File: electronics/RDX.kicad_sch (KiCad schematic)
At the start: 47 parts

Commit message: updating electronics to fit new outline
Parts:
- removed OUT.POW: Conn_01x06, symbol Connector_Generic:Conn_01x06
- added A7.J1_1, A7.J1_2, A7.J1_3: Anderson SB50, symbol Connector_Generic:Conn_01x02
- A6.J1_1: renamed from OUT.SV1; value Conn_01x03 -> GX12-3
- A6.J1_2: renamed from OUT.SV2; value Conn_01x03 -> GX12-3
- A6.J1_3: renamed from OUT.SV3; value Conn_01x03 -> GX12-3
- A6.J1_4: renamed from OUT.SV4; value Conn_01x03 -> GX12-3
- A6.J1_5: renamed from OUT.SV5; value Conn_01x03 -> GX12-3
- A6.J1_6: renamed from OUT.SV6; value Conn_01x03 -> GX12-3
- A9.J1_1: renamed from OUT.STEP1; value Conn_01x04 -> GX16-4
- renumbered A4.J1_21 to A4.J1_3, A4.J1_21 to A4.J1_4, PSU.J31 to A4.J1_5, PSU.J32 to A4.J1_6, PSU.J41 to A4.J2_1, A4.J12 to A4.J3_2, A4.PS11 to A4.PS1, A4.PS12 to A4.PS2, A4.PS13 to A4.PS3, OUT.IO1 to A5.J1_1, OUT.IO2 to A5.J1_2, OUT.MISC to A5.J1_3, OUT.SW2 to A8.SW1, OUT.SW1 to A8.SW2, OUT.U1 to A8.U1, OUT.STEP2 to A9.J1_2, OUT.STEP3 to A9.J1_3, OUT.STEP4 to A9.J1_4, PSU.J1 to J1, OUT.M1 to M1, A4.PS1 to PS1, PSU.SW1 to SW1
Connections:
- net +12V: now also A7.J1_2.1 (Pin_1)
- net +36V: now also A7.J1_1.1 (Pin_1)
- net 5V_PWR: now also A7.J1_3.1 (Pin_1)
- net GND: now also A7.J1_1.2 (Pin_2), A7.J1_2.2 (Pin_2), A7.J1_3.2 (Pin_2)
- new net: A2.J1_2., A2.U1_2. (B2) (x3)
- new net: A2.J1_4., A2.U1_4. (B2) (x3)
- new net: A2.J1_1., A2.U1_1. (B2) (x3)
- new net: A2.J1_3., A2.U1_3. (B2) (x3)
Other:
- note added: "A4.J1_3 (12V)"
- note added: "A4.J2_1 (5V)"
- note added: "A4.J3_1 (36V)"
- note added: "A5 - GPIO Connectors"
- note added: "A5.J1_2 - Special functions"
- note added: "A5.J1_3 - Special functions"
- note added: "A7 - Power connector"
- note added: "A8 - Input panel"
- note added: "Main PSU (A4.PS1) supports up to 3 connections"
- note removed: "IO2 - Special functions"
- note removed: "MISC - Special functions"
- note removed: "Main PSU (PSU.PS1) supports up to 3 connections"
- note removed: "PSU.J12 (36V)"
- note removed: "PSU.J22 (12V)"
- note removed: "PSU.J32 (5V)"
- moved on the sheet: A5.J1_1, A5.J1_2, A5.J1_3, A6.J1_1, A6.J1_2, A6.J1_3, A6.J1_4, A6.J1_5, A6.J1_6, A8.U1, M1

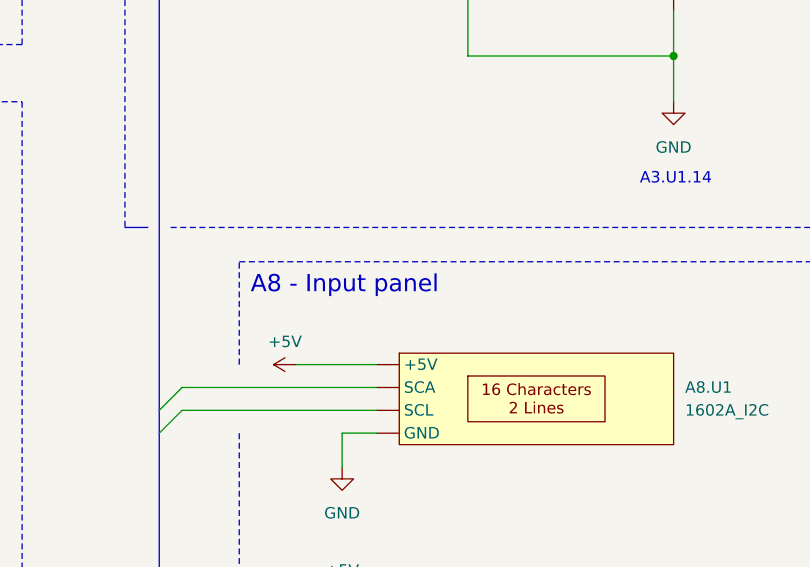
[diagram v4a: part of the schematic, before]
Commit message: first addition of screws
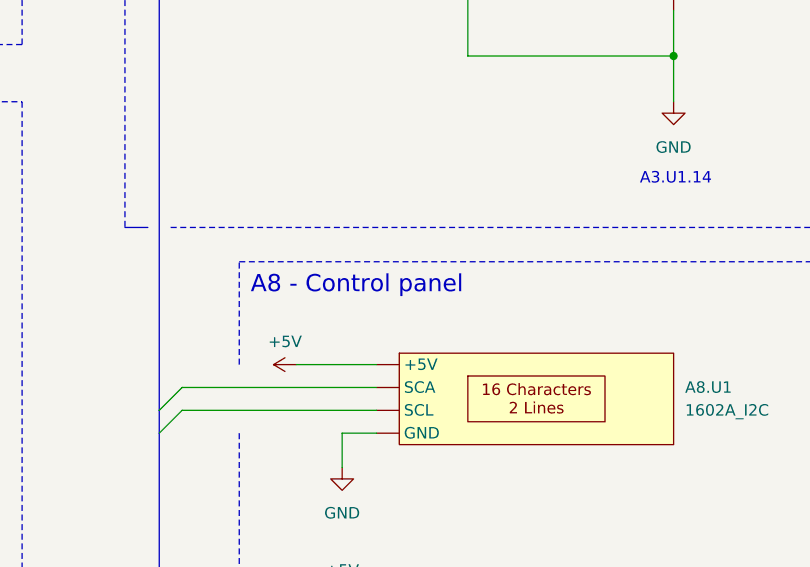
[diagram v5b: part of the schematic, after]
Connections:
- new net: A2.J1_2., A2.U1_2. (B2) (x3)
- new net: A2.J1_4., A2.U1_4. (B2) (x3)
- new net: A2.J1_1., A2.U1_1. (B2) (x3)
- new net: A2.J1_3., A2.U1_3. (B2) (x3)
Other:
- note added: "A8 - Control panel"
- note removed: "A8 - Input panel"
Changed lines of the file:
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@@
 		(title "RDX - Robot Driver Mk.X")
 		(date "2026-04-01")
-		(rev "1.2.0")
+		(rev "1.2.1")
 		(company "CornerLab")
 		(comment 1 "Universal Robot Driver")
@@
 		)
 	)
-	(text "A8 - Input panel"
+	(text "A8 - Control panel"
 		(exclude_from_sim no)
 		(at 191.77 203.454 0)

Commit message: schematics and electronics cleanup
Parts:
- removed A6.J1_1, A6.J1_2, A6.J1_3, A6.J1_4, A6.J1_5, A6.J1_6: GX12-3, symbol Connector_Generic:Conn_01x03
- removed A8.SW1: SW_SPST, symbol Switch:SW_SPST
- removed A9.J1_1: GX16-4, symbol Connector_Generic:Conn_01x04
- removed A9.J1_2, A9.J1_3, A9.J1_4: Conn_01x04, symbol Connector_Generic:Conn_01x04
- removed M1: Fan_4pin, symbol Motor:Fan_4pin
- added A10.J1_1, A10.J1_2, A10.J1_3: GX16-2, symbol Connector:Conn_01x02_Pin
- added A11.J1_1, A11.J1_2, A11.J1_3, A11.J1_4: GX16-4, symbol Connector:Conn_01x04_Pin
- added A3.J2, A3.J3: ~, symbol RDX_Comp:Conn_01-02
- added A3.J3_1: ~, symbol RDX_Comp:Conn_01-04
- added A5.U1_1, A5.U1_2: JoyIt-MotorDriver2, symbol RDX_Comp:JoyIt-MotorDriver2
- added A6.J1_1, A6.J1_2, A6.J1_3, A6.J1_4, A6.J1_5, A6.J1_6, A6.J1_7, A6.J1_8: GX12-3, symbol Connector:Conn_01x03_Pin
- added M1: Fan_3pin, symbol Motor:Fan_3pin
- renumbered A3.J3 to A3.J3_2, A4.PS1 to A4.PS1_1, A4.PS2 to A4.PS1_2, A4.PS3 to A4.PS2, A5.J1_1 to A6.J1_1, A5.J1_2 to A6.J1_2, A5.J1_3 to A6.J1_3
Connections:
- net MISC_5V is gone; now on net +5V: A3.U1.4 (+5V), A6.J1_3.1
- net +12V: now also A5.U1_2. (B2)
- net +36V: now also A3.J2.
- net 5V_PWR: now also A6.J1_1.2 (Pin_2), A6.J1_2.2 (Pin_2), A6.J1_3.2 (Pin_2), A6.J1_4.2 (Pin_2), A6.J1_5.2 (Pin_2), A6.J1_6.2 (Pin_2), A6.J1_7.2 (Pin_2), A6.J1_8.2 (Pin_2)
- net GND: now also A3.J3., A5.U1_2. (B2), A6.J1_1.3 (Pin_3), A6.J1_2.3 (Pin_3), A6.J1_3.3 (Pin_3), A6.J1_4.3 (Pin_3), A6.J1_5.3 (Pin_3), A6.J1_6.3 (Pin_3), A6.J1_7.3 (Pin_3), A6.J1_8.3 (Pin_3)
- net SC_EN: now also A3.J3_1.; no longer A3.U1.29 (IO5)
- net at A3.U2.9 (LED3): now also A6.J1_4.1 (Pin_1)
- net at A4.J1_1., A4.PS1_1.3 (+VIN), PS1.3 (DC+): now also A4.J3_1.
- net at A3.U2.10 (LED4): now also A6.J1_5.1 (Pin_1)
- net at A3.U2.11 (LED5): now also A6.J1_6.1 (Pin_1)
- net at A3.U2.12 (LED6): now also A6.J1_7.1 (Pin_1)
- net at A3.U2.13 (LED7): now also A6.J1_8.1 (Pin_1)
- net DC1_FW: now reaches A3.U2.15 (LED8)
- net DC1_FW: now also A5.U1_1. (B2)
- net DC1_BW: now reaches A3.U2.16 (LED9)
- net DC1_BW: now also A5.U1_1. (B2)
- net DC2_FW: now reaches A3.U2.17 (LED10)
- net DC2_FW: now also A5.U1_1. (B2)
- net DC2_BW: now reaches A3.U2.18 (LED11)
- net DC2_BW: now also A5.U1_1. (B2)
- net DC3_FW: now reaches A3.U2.19 (LED12)
- net DC3_FW: now also A5.U1_2. (B2)
- net DC3_BW: now reaches A3.U2.20 (LED13)
- net DC3_BW: now also A5.U1_2. (B2)
- net FAN_FW: now reaches A3.U2.21 (LED14)
- net FAN_FW: now also A5.U1_2. (B2)
- net FAN_BW: now reaches A3.U2.22 (LED15)
- net FAN_BW: now also A5.U1_2. (B2)
- net at A3.U2.6 (LED0): now also A6.J1_1.1 (Pin_1)
- net at A3.U2.7 (LED1): now also A6.J1_2.1 (Pin_1)
- net at A3.U2.8 (LED2): now also A6.J1_3.1 (Pin_1)
- new net: A11.J1_4.1 (Pin_1), A2.U1_4. (B2)
- new net: A11.J1_4.2 (Pin_2), A2.U1_4. (B2)
- new net: A11.J1_4.3 (Pin_3), A2.U1_4. (B2)
- new net: A11.J1_4.4 (Pin_4), A2.U1_4. (B2)
- new net: A11.J1_3.1 (Pin_1), A2.U1_3. (B2)
- new net: A11.J1_3.2 (Pin_2), A2.U1_3. (B2)
- new net: A11.J1_3.3 (Pin_3), A2.U1_3. (B2)
- new net: A11.J1_3.4 (Pin_4), A2.U1_3. (B2)
- new net: A2.J1_2., A2.U1_2. (B2) (x3)
- new net: A2.J1_4., A2.U1_4. (B2) (x3)
- new net: A10.J1_1.1 (Pin_1), A5.U1_1. (B2)
- new net: A10.J1_1.2 (Pin_2), A5.U1_1. (B2)
- new net: A10.J1_2.1 (Pin_1), A5.U1_1. (B2)
- new net: A10.J1_2.2 (Pin_2), A5.U1_1. (B2)
- new net: A3.J3., A5.U1_1. (B2)
- new net: A3.J2., A5.U1_1. (B2)
- new net: A2.J1_1., A2.U1_1. (B2) (x3)
- new net: A5.U1_2. (B2), M1.1 (-)
- new net: A5.U1_2. (B2), M1.2 (+)
- new net: A3.J3_1., A3.U1.29 (IO5)
- new net: A11.J1_1.1 (Pin_1), A2.U1_1. (B2)
- new net: A11.J1_1.2 (Pin_2), A2.U1_1. (B2)
- new net: A11.J1_1.3 (Pin_3), A2.U1_1. (B2)
- new net: A11.J1_1.4 (Pin_4), A2.U1_1. (B2)
- new net: A2.J1_3., A2.U1_3. (B2) (x3)
- new net: A10.J1_3.1 (Pin_1), A5.U1_2. (B2)
- new net: A10.J1_3.2 (Pin_2), A5.U1_2. (B2)
- new net: A11.J1_2.1 (Pin_1), A2.U1_2. (B2)
- new net: A11.J1_2.2 (Pin_2), A2.U1_2. (B2)
- new net: A11.J1_2.3 (Pin_3), A2.U1_2. (B2)
- new net: A11.J1_2.4 (Pin_4), A2.U1_2. (B2)
- no-connect marks 17 -> 6
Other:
- note added: "A2 - PANEL I - Stepper panel"
- note added: "A3.U1.4"
- note added: "A4.J1_6 (5V PWR)"
- note added: "A5 - DC-Motor panel"
- note added: "A6 - GPIO Connectors"
- note added: "A8 - Power connectors"
- note added: "A8 - User panel"
- note removed: "A2 - PANEL I - Stepper Panel"
- note removed: "A4.J32 (5V PWR)"
- note removed: "A5 - GPIO Connectors"
- note removed: "A7 - Power connector"
- note removed: "A8 - Control panel"
- moved on the sheet: A3.J1, A3.J2_1, A3.J2_2, A3.J3_2, A3.U1, A3.U2, A6.J1_1, A6.J1_2, A6.J1_3, A7.J1_1, A7.J1_2, A7.J1_3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

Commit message: updating electronics to RPi hat and adding more outlines
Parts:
- removed A3.U1: RPi_Generic, symbol RDX_Comp:RPi_Board
- added A3.U1: RPi_Terminal_Hat, symbol RDX_Comp:RPi_Terminal_Hat
- A5.U1_1, A5.U1_2: value JoyIt-MotorDriver2 -> L298N
- renumbered A6.J1_1 to A7.J1_1, A6.J1_2 to A7.J1_2, A6.J1_3 to A7.J1_3, A6.J1_4 to A7.J1_4, A6.J1_5 to A7.J1_5, A6.J1_6 to A7.J1_6, A6.J1_7 to A7.J1_7, A6.J1_8 to A7.J1_8
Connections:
- net +5V: now also A3.U1.2 (+5V), A3.U1.4 (+5V)
- net GND: now also A3.U1.14 (GND), A3.U1.30 (GND), A3.U1.39 (GND), A3.U1.6 (GND)
- net IO1_1: now also A3.U1.7 (IO4)
- net IO1_2: now also A3.U1.13 (IO27)
- net IO1_3: now also A3.U1.40 (IO21)
- net IO1_4: now also A3.U1.33 (IO13)
- net IO1_GND: now also A3.U1.20 (GND)
- net IO2_1: now also A3.U1.19 (IO10)
- net IO2_2: now also A3.U1.21 (IO9)
- net IO2_3: now also A3.U1.23 (IO11)
- net IO2_4: now also A3.U1.24 (IO8)
- net IO2_GND: now also A3.U1.9 (GND)
- net MISC_3.3V: now also A3.U1.17 (+3.3V)
- net MISC_CS1: now also A3.U1.26 (IO7)
- net MISC_GND: now also A3.U1.25 (GND)
- net MISC_RX: now also A3.U1.12 (IO15)
- net MISC_TX: now also A3.U1.8 (IO14)
- net ROT_CL: now also A3.U1.12 (IO15)
- net ROT_DT: now also A3.U1.11 (IO17)
- net ROT_SW: now also A3.U1.35 (IO19)
- net SC1_DIR: now also A3.U1.16 (IO23)
- net SC1_STEP: now also A3.U1.18 (IO24)
- net SC2_DIR: now also A3.U1.15 (IO22)
- net SC2_STEP: now also A3.U1.22 (IO25)
- net SC3_DIR: now also A3.U1.32 (IO12)
- net SC3_STEP: now also A3.U1.29 (IO5)
- net SC4_DIR: now also A3.U1.38 (IO20)
- net SC4_STEP: now also A3.U1.31 (IO6)
- net SCL: now also A3.U1.5 (IO3)
- net SDA: now also A3.U1.3 (IO2)
- new net: A3.J3_2., A3.U1.34 (GND)
- new net: A2.J1_2., A2.U1_2. (B2) (x3)
- new net: A2.J1_4., A2.U1_4. (B2) (x3)
- new net: A3.J3., A5.U1_1. (B2)
- new net: A3.J2., A5.U1_1. (B2)
- new net: A2.J1_1., A2.U1_1. (B2) (x3)
- new net: A3.J1., A3.U1.1 (+3.3V)
- new net: A3.J3_1., A3.U1.36 (IO16)
- new net: A2.J1_3., A2.U1_3. (B2) (x3)
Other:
- note added: "A6.J1_1 - Connection"
- note added: "A6.J1_2 - Special functions"
- note added: "A6.J1_3 - Special functions"
- note added: "Power supply"
- note removed: "A5.J1_2 - Special functions"
- note removed: "A5.J1_3 - Special functions"
- note removed: "Power connection from PSU"
- moved on the sheet: A3.J1, A3.J2_1, A3.J2_2, A3.J3_1, A3.J3_2

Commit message: electronics update to 1.3.0
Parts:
- removed A8.U1: 1602A_I2C, symbol RDX_Comp:LCD1602A_I2C
- added A9.BZ1: Buzzer, symbol Device:Buzzer
- added A9.U1: LCD2004_I2C, symbol RDX_Comp:LCD2004_I2C
- renumbered A8.SW2 to A9.SW1
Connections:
- net +5V: now also A9.U1. (GND)
- net GND: now also A9.BZ1.2 (-), A9.U1. (GND)
- net BUZZER: now reaches A3.U1.37 (IO26)
- net BUZZER: now also A9.BZ1.1 (+)
- new net: A2.J1_2., A2.U1_2. (B2) (x3)
- new net: A2.J1_4., A2.U1_4. (B2) (x3)
- new net: A3.J3., A5.U1_1. (B2)
- new net: A3.J2., A5.U1_1. (B2)
- new net: A2.J1_1., A2.U1_1. (B2) (x3)
- new net: A2.J1_3., A2.U1_3. (B2) (x3)
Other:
- note added: "A9 - User panel"
- note removed: "A8 - User panel"
- moved on the sheet: A9.SW1
